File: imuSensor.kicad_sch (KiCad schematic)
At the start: 3 parts, among them U1 LSM6DSV

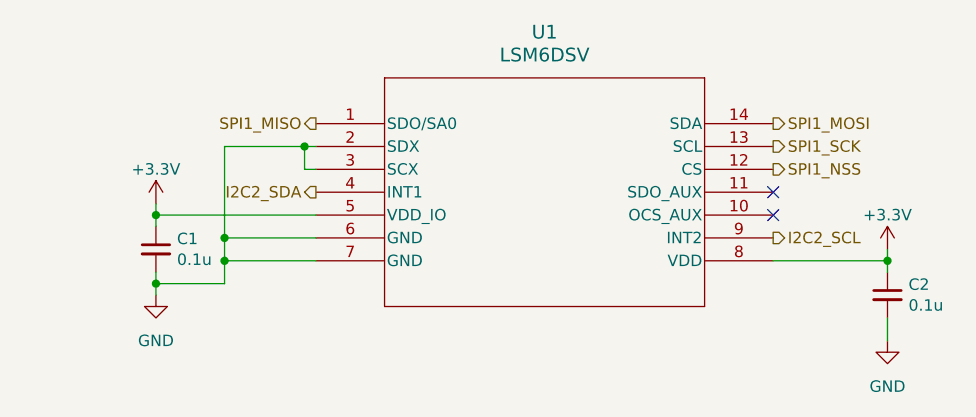
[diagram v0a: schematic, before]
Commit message: fixed spi1_nss conflict, switched imu to spi2
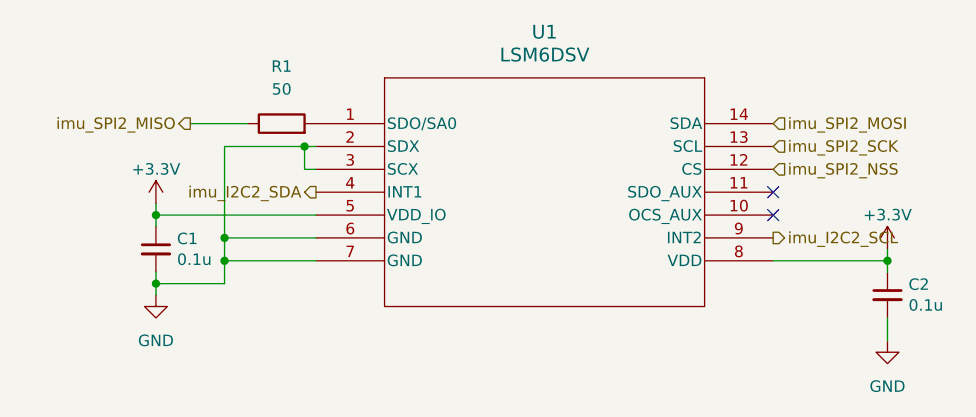
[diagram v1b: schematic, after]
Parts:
- added R1: 50, Resistor_SMD:R_0805_2012Metric, symbol Device:R
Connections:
- net I2C2_SCL renamed imu_I2C2_SCL
- net I2C2_SDA renamed imu_I2C2_SDA
- net SPI1_MISO: no longer names the net of U1.1 (SDO/SA0)
- net SPI1_MISO: now also R1.2
- net SPI1_MOSI renamed imu_SPI2_MOSI
- net SPI1_NSS renamed imu_SPI2_NSS
- net SPI1_SCK renamed imu_SPI2_SCK
- new net imu_SPI2_MISO: R1.1
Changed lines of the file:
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@@
+    (stroke (width 0) (type default))
+  )
+  (wire (pts (xy 101.6 83.82) (xy 107.95 83.82))
     (stroke (width 0) (type default))
   )
@@
     (stroke (width 0) (type default))
   )
-  (hierarchical_label "I2C2_SCL" (shape output) (at 166.37 96.52 0) (fields_autoplaced)
-    (effects (font (size 1.27 1.27)) (justify left))
-  )
-  (hierarchical_label "I2C2_SDA" (shape output) (at 115.57 91.44 180) (fields_autoplaced)
+  (hierarchical_label "imu_I2C2_SCL" (shape output) (at 166.37 96.52 0) (fields_autoplaced)
+    (effects (font (size 1.27 1.27)) (justify left))
+  )
+  (hierarchical_label "imu_I2C2_SDA" (shape output) (at 115.57 91.44 180) (fields_autoplaced)
     (effects (font (size 1.27 1.27)) (justify right))
   )
-  (hierarchical_label "SPI1_SCK" (shape output) (at 166.37 86.36 0) (fields_autoplaced)
-    (effects (font (size 1.27 1.27)) (justify left))
-  )
-  (hierarchical_label "SPI1_MISO" (shape output) (at 115.57 83.82 180) (fields_autoplaced)
+  (hierarchical_label "imu_SPI2_SCK" (shape input) (at 166.37 86.36 0) (fields_autoplaced)
+    (effects (font (size 1.27 1.27)) (justify left))
+  )
+  (hierarchical_label "imu_SPI2_MISO" (shape output) (at 101.6 83.82 180) (fields_autoplaced)
     (effects (font (size 1.27 1.27)) (justify right))
   )
-  (hierarchical_label "SPI1_MOSI" (shape output) (at 166.37 83.82 0) (fields_autoplaced)
-    (effects (font (size 1.27 1.27)) (justify left))
-  )
-  (hierarchical_label "SPI1_NSS" (shape output) (at 166.37 88.9 0) (fields_autoplaced)
+  (hierarchical_label "imu_SPI2_MOSI" (shape input) (at 166.37 83.82 0) (fields_autoplaced)
+    (effects (font (size 1.27 1.27)) (justify left))
+  )
+  (hierarchical_label "imu_SPI2_NSS" (shape input) (at 166.37 88.9 0) (fields_autoplaced)
     (effects (font (size 1.27 1.27)) (justify left))
   )
@@
         )
       )
+    )
+  )
+  (symbol (lib_id "Device:R") (at 111.76 83.82 90) (unit 1)
+    (in_bom yes) (on_board yes) (dnp no) (fields_autoplaced)
+    (property "Reference" "R1" (at 111.76 77.47 90)
+      (effects (font (size 1.27 1.27)))
+    )
+    (property "Value" "50" (at 111.76 80.01 90)
+      (effects (font (size 1.27 1.27)))
+    )
+    (property "Footprint" "Resistor_SMD:R_0805_2012Metric" (at 111.76 85.598 90)
+      (effects (font (size 1.27 1.27)) hide)
+    )
+    (property "Datasheet" "~" (at 111.76 83.82 0)
+      (effects (font (size 1.27 1.27)) hide)
+    )
+    (pin "1")
+    (pin "2")
+    (instances
+      (project "Telemetry-Peripheral-SOM-Daughterboard-IMU"
+        (path "/637f68f0-cb9c-412a-8573-5d8e7ef6d8a2/1c44fd59-b97c-4be4-9bf8-a0e08d703171"
+          (reference "R1") (unit 1)
+        )
+      )

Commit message: first draft
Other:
- note added: "IMU Sensor"
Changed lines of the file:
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@@
     (stroke (width 0) (type default))
+  )
+  (text "IMU Sensor\n" (at 15.24 24.13 0)
+    (effects (font (size 5 5) (thickness 1) bold) (justify left bottom))
   )
   (hierarchical_label "imu_I2C2_SCL" (shape output) (at 166.37 96.52 0) (fields_autoplaced)
@@
         )
         (path "/637f68f0-cb9c-412a-8573-5d8e7ef6d8a2/1c44fd59-b97c-4be4-9bf8-a0e08d703171"
-          (reference "C10") (unit 1)
+          (reference "C2") (unit 1)
         )
       )
@@
         )
         (path "/637f68f0-cb9c-412a-8573-5d8e7ef6d8a2/1c44fd59-b97c-4be4-9bf8-a0e08d703171"
-          (reference "C9") (unit 1)
+          (reference "C1") (unit 1)
         )
       )
@@
         )
         (path "/637f68f0-cb9c-412a-8573-5d8e7ef6d8a2/1c44fd59-b97c-4be4-9bf8-a0e08d703171"
-          (reference "U2") (unit 1)
-        )
-      )
+          (reference "U1") (unit 1)
+        )
+      )

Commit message: fixes
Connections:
- net imu_I2C2_SCL renamed INT2
- net imu_I2C2_SDA renamed INT1
- net imu_SPI2_MISO renamed SDO/SA0
- net imu_SPI2_MOSI renamed SDA
- net imu_SPI2_NSS renamed CS
- net imu_SPI2_SCK renamed SCL
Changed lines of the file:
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@@
     (effects (font (size 5 5) (thickness 1) bold) (justify left bottom))
   )
-  (hierarchical_label "imu_I2C2_SCL" (shape output) (at 166.37 96.52 0) (fields_autoplaced)
+  (hierarchical_label "INT2" (shape output) (at 166.37 96.52 0) (fields_autoplaced)
     (effects (font (size 1.27 1.27)) (justify left))
   )
-  (hierarchical_label "imu_I2C2_SDA" (shape output) (at 115.57 91.44 180) (fields_autoplaced)
+  (hierarchical_label "INT1" (shape output) (at 115.57 91.44 180) (fields_autoplaced)
     (effects (font (size 1.27 1.27)) (justify right))
   )
-  (hierarchical_label "imu_SPI2_SCK" (shape input) (at 166.37 86.36 0) (fields_autoplaced)
+  (hierarchical_label "SCL" (shape input) (at 166.37 86.36 0) (fields_autoplaced)
     (effects (font (size 1.27 1.27)) (justify left))
   )
-  (hierarchical_label "imu_SPI2_MISO" (shape output) (at 101.6 83.82 180) (fields_autoplaced)
+  (hierarchical_label "SDO{slash}SA0" (shape output) (at 101.6 83.82 180) (fields_autoplaced)
     (effects (font (size 1.27 1.27)) (justify right))
   )
-  (hierarchical_label "imu_SPI2_MOSI" (shape input) (at 166.37 83.82 0) (fields_autoplaced)
+  (hierarchical_label "SDA" (shape input) (at 166.37 83.82 0) (fields_autoplaced)
     (effects (font (size 1.27 1.27)) (justify left))
   )
-  (hierarchical_label "imu_SPI2_NSS" (shape input) (at 166.37 88.9 0) (fields_autoplaced)
+  (hierarchical_label "CS" (shape input) (at 166.37 88.9 0) (fields_autoplaced)
     (effects (font (size 1.27 1.27)) (justify left))
   )

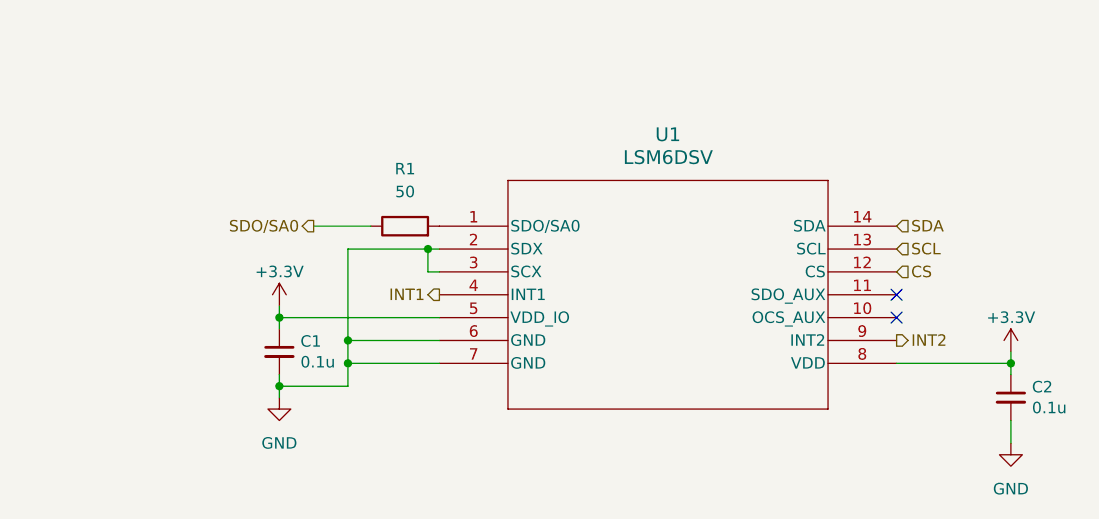
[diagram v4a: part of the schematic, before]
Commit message: added protective circuitry for temp sensors, made name changes for IMU
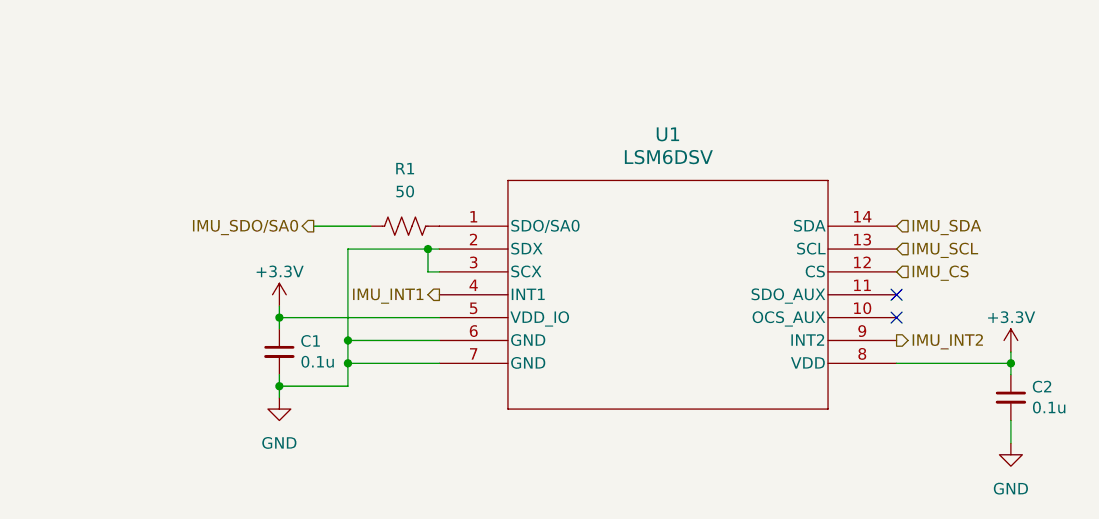
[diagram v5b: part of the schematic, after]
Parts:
- removed R1: 50, Resistor_SMD:R_0805_2012Metric, symbol Device:R
- added R1: 50, symbol Device:R_US
- U1: Mouser Part Number (none) -> 511-LSM6DSV16BTR; P/N LSM6DSV -> LSM6DSV16BTR
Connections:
- net at U1.1 (SDO/SA0): now also R1.2
- net CS renamed IMU_CS
- net INT1 renamed IMU_INT1
- net INT2 renamed IMU_INT2
- net SCL renamed IMU_SCL
- net SDA renamed IMU_SDA
- new net IMU_SDO/SA0: R1.1
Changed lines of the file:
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@@
     (effects (font (size 5 5) (thickness 1) bold) (justify left bottom))
   )
-  (hierarchical_label "INT2" (shape output) (at 166.37 96.52 0) (fields_autoplaced)
-    (effects (font (size 1.27 1.27)) (justify left))
-  )
-  (hierarchical_label "INT1" (shape output) (at 115.57 91.44 180) (fields_autoplaced)
+  (hierarchical_label "IMU_INT2" (shape output) (at 166.37 96.52 0) (fields_autoplaced)
+    (effects (font (size 1.27 1.27)) (justify left))
+  )
+  (hierarchical_label "IMU_INT1" (shape output) (at 115.57 91.44 180) (fields_autoplaced)
     (effects (font (size 1.27 1.27)) (justify right))
   )
-  (hierarchical_label "SCL" (shape input) (at 166.37 86.36 0) (fields_autoplaced)
-    (effects (font (size 1.27 1.27)) (justify left))
-  )
-  (hierarchical_label "SDO{slash}SA0" (shape output) (at 101.6 83.82 180) (fields_autoplaced)
+  (hierarchical_label "IMU_SCL" (shape input) (at 166.37 86.36 0) (fields_autoplaced)
+    (effects (font (size 1.27 1.27)) (justify left))
+  )
+  (hierarchical_label "IMU_SDO{slash}SA0" (shape output) (at 101.6 83.82 180) (fields_autoplaced)
     (effects (font (size 1.27 1.27)) (justify right))
   )
-  (hierarchical_label "SDA" (shape input) (at 166.37 83.82 0) (fields_autoplaced)
-    (effects (font (size 1.27 1.27)) (justify left))
-  )
-  (hierarchical_label "CS" (shape input) (at 166.37 88.9 0) (fields_autoplaced)
+  (hierarchical_label "IMU_SDA" (shape input) (at 166.37 83.82 0) (fields_autoplaced)
+    (effects (font (size 1.27 1.27)) (justify left))
+  )
+  (hierarchical_label "IMU_CS" (shape input) (at 166.37 88.9 0) (fields_autoplaced)
     (effects (font (size 1.27 1.27)) (justify left))
   )
@@
       (effects (font (size 1.27 1.27) italic) hide)
     )
-    (property "P/N" "LSM6DSV" (at 118.11 74.93 0)
+    (property "P/N" "LSM6DSV16BTR" (at 118.11 74.93 0)
+      (effects (font (size 1.27 1.27)) hide)
+    )
+    (property "Mouser Part Number" "511-LSM6DSV16BTR" (at 115.57 83.82 0)
       (effects (font (size 1.27 1.27)) hide)
     )
@@
     )
   )
-  (symbol (lib_id "Device:R") (at 111.76 83.82 90) (unit 1)
+  (symbol (lib_id "Device:R_US") (at 111.76 83.82 90) (unit 1)
     (in_bom yes) (on_board yes) (dnp no) (fields_autoplaced)
     (property "Reference" "R1" (at 111.76 77.47 90)
@@
       (effects (font (size 1.27 1.27)))
     )
-    (property "Footprint" "Resistor_SMD:R_0805_2012Metric" (at 111.76 85.598 90)
-      (effects (font (size 1.27 1.27)) hide)
-    )
+    (property "Footprint" "" (at 112.014 82.804 90)
+      (effects (font (size 1.27 1.27)) hide)
+    )

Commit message: Name changes
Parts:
- R1: footprint (none) -> Resistor_SMD:R_0805_2012Metric
- U1: Mouser Part Number 511-LSM6DSV16BTR -> 511-LSM6DSVTR; P/N LSM6DSV16BTR -> LSM6DSVTR
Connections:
- net IMU_SCL renamed IMU_MOSI
- net IMU_SDA renamed IMU_SCK
- net IMU_SDO/SA0 renamed IMU_MISO
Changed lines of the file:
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@@
     (effects (font (size 1.27 1.27)) (justify right))
   )
-  (hierarchical_label "IMU_SCL" (shape input) (at 166.37 86.36 0) (fields_autoplaced)
+  (hierarchical_label "IMU_MOSI" (shape input) (at 166.37 86.36 0) (fields_autoplaced)
     (effects (font (size 1.27 1.27)) (justify left))
   )
-  (hierarchical_label "IMU_SDO{slash}SA0" (shape output) (at 101.6 83.82 180) (fields_autoplaced)
+  (hierarchical_label "IMU_MISO" (shape output) (at 101.6 83.82 180) (fields_autoplaced)
     (effects (font (size 1.27 1.27)) (justify right))
   )
-  (hierarchical_label "IMU_SDA" (shape input) (at 166.37 83.82 0) (fields_autoplaced)
+  (hierarchical_label "IMU_SCK" (shape input) (at 166.37 83.82 0) (fields_autoplaced)
     (effects (font (size 1.27 1.27)) (justify left))
   )
@@
       (effects (font (size 1.27 1.27) italic) hide)
     )
-    (property "P/N" "LSM6DSV16BTR" (at 118.11 74.93 0)
-      (effects (font (size 1.27 1.27)) hide)
-    )
-    (property "Mouser Part Number" "511-LSM6DSV16BTR" (at 115.57 83.82 0)
+    (property "P/N" "LSM6DSVTR" (at 118.11 74.93 0)
+      (effects (font (size 1.27 1.27)) hide)
+    )
+    (property "Mouser Part Number" "511-LSM6DSVTR" (at 115.57 83.82 0)
       (effects (font (size 1.27 1.27)) hide)
     )
@@
       (effects (font (size 1.27 1.27)))
     )
-    (property "Footprint" "" (at 112.014 82.804 90)
-      (effects (font (size 1.27 1.27)) hide)
-    )
+    (property "Footprint" "Resistor_SMD:R_0805_2012Metric" (at 112.014 82.804 90)
+      (effects (font (size 1.27 1.27)) hide)
+    )

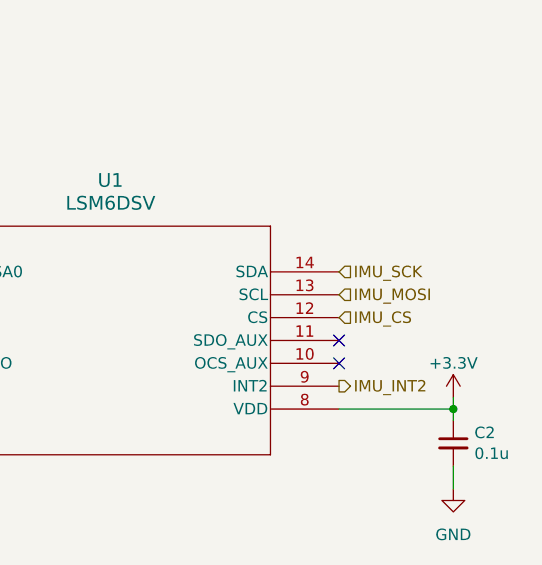
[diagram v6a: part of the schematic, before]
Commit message: Changes to routing and silkscreen, addressed schematic error
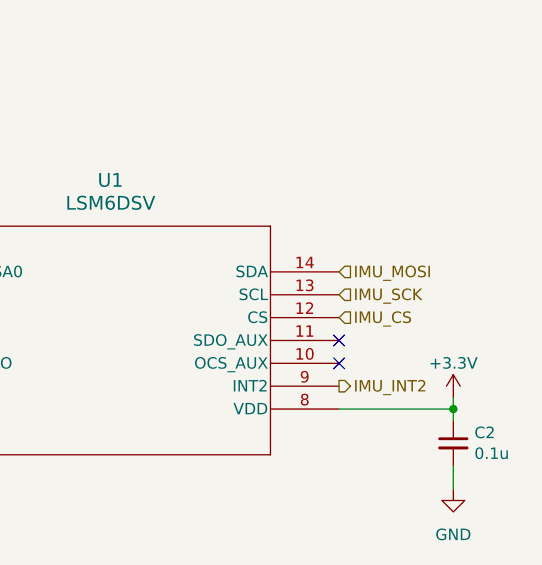
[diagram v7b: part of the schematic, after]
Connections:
- net IMU_MOSI: now also U1.14 (SDA); no longer U1.13 (SCL)
- net IMU_SCK: now also U1.13 (SCL); no longer U1.14 (SDA)
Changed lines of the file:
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@@
     (effects (font (size 1.27 1.27)) (justify right))
   )
-  (hierarchical_label "IMU_MOSI" (shape input) (at 166.37 86.36 0) (fields_autoplaced)
+  (hierarchical_label "IMU_MOSI" (shape input) (at 166.37 83.82 0) (fields_autoplaced)
     (effects (font (size 1.27 1.27)) (justify left))
   )
@@
     (effects (font (size 1.27 1.27)) (justify right))
   )
-  (hierarchical_label "IMU_SCK" (shape input) (at 166.37 83.82 0) (fields_autoplaced)
+  (hierarchical_label "IMU_SCK" (shape input) (at 166.37 86.36 0) (fields_autoplaced)
     (effects (font (size 1.27 1.27)) (justify left))
   )
